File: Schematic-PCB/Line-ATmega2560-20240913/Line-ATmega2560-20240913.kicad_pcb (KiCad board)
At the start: 2 copper layers, 27 parts, among them J6 CH340E, J7 ICSP, SW1 SW_Push, U1 ATmega2560-16A, Y1 16MHz

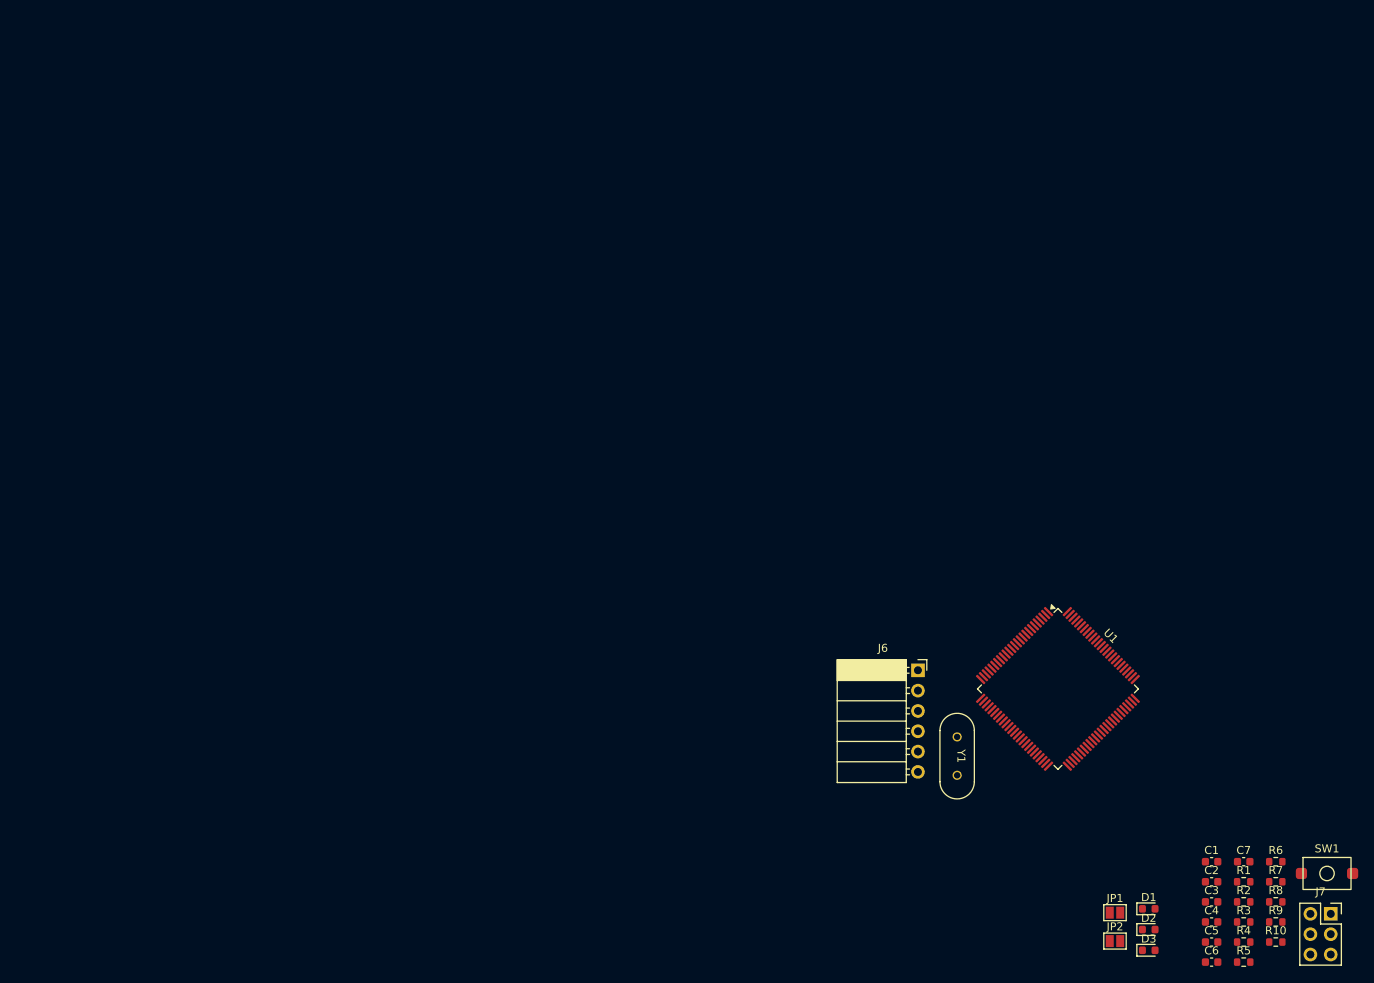
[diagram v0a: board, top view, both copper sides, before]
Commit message: 評価基板のPCB仮完成
各ピンを出す用のコネクタ以外は配置・配線完了
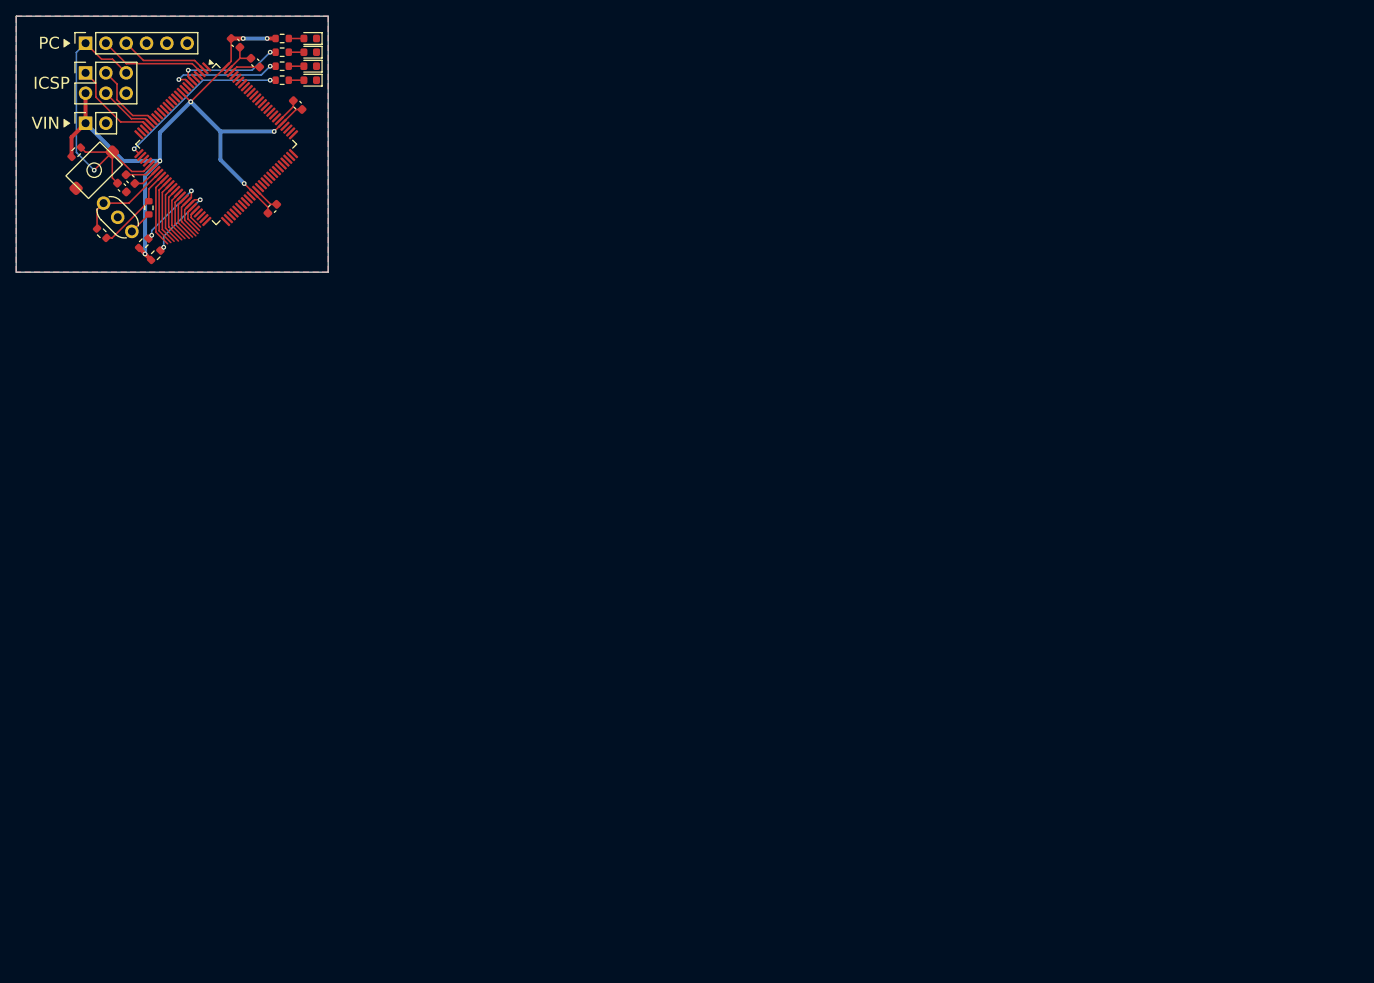
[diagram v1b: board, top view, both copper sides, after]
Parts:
- removed C7: 22p, Capacitor_SMD:C_0603_1608Metric
- removed J6: CH340E, Connector_PinSocket_2.54mm:PinSocket_1x06_P2.54mm_Horizontal
- removed J7: ICSP, Connector_PinSocket_2.54mm:PinSocket_2x03_P2.54mm_Vertical
- removed JP1: W_R, Jumper:SolderJumper-2_P1.3mm_Open_Pad1.0x1.5mm
- removed JP2: W/O_R, Jumper:SolderJumper-2_P1.3mm_Open_Pad1.0x1.5mm
- removed R10: 10K, Resistor_SMD:R_0603_1608Metric
- added D4: LED1, LED_SMD:LED_0603_1608Metric, F.Cu at (11.6, -8.29)
- added J10: VIN, Connector_PinSocket_2.54mm:PinSocket_1x02_P2.54mm_Vertical, F.Cu at (-16.4, -2.91)
- added J8: CH340E, Connector_PinSocket_2.54mm:PinSocket_1x06_P2.54mm_Vertical, F.Cu at (-16.4, -12.9)
- added J9: ICSP, Connector_PinSocket_2.54mm:PinSocket_2x03_P2.54mm_Vertical, F.Cu at (-16.4, -9.20)
- C6: value 22p -> 100n
- R7: value 10K -> 27
- R8: value 27R -> 330
- Y1: footprint @2024TOINIOT2-Line-ATmega2560:AL4BT -> Crystal:Resonator_Murata_CSTLSxxxX-3Pin_W5.5mm_H3.0mm
- moved SW1 177.4 mm to (-15.4, 2.96), turned to -135 degrees
- moved R2 173.4 mm to (-17.6, 0.71), turned to 45 degrees
- moved R9 170.1 mm to (-14.4, 10.8), turned to 135 degrees
- moved R5 164.3 mm to (-9.18, 12.1), turned to 45 degrees
- moved R7 164.1 mm to (-8.54, 7.67), turned to -90 degrees
- moved C4 164.0 mm to (-10.8, 4.07), turned to -45 degrees
- moved R4 162.6 mm to (8.13, -10.0)
- moved C3 162.5 mm to (2.30, -13.0), turned to -45 degrees
- moved R3 162.1 mm to (8.13, -11.8)
- moved C2 161.5 mm to (-11.9, 5.13), turned to -45 degrees
- moved R8 161.2 mm to (8.13, -8.29)
- moved R1 159.9 mm to (8.13, -13.5)
- moved R6 159.2 mm to (-7.68, 13.6), turned to 45 degrees
- moved C6 156.6 mm to (10.1, -5.18), turned to 135 degrees
- moved C1 155.8 mm to (4.77, -10.5), turned to -45 degrees
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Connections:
- C6 pad 1: Net-(JP2-B) -> +5V
- R7 pad 1: +5V -> XTAL1
- R7 pad 2: Net-(SW2-A) -> Net-(R7-Pad2)
- R8 pad 1: Net-(JP1-B) -> D13
- R8 pad 2: Net-(JP2-B) -> Net-(D4-A)
- R9 pad 1: Net-(JP2-B) -> XTAL1
- U1 pad 82: D42 -> ADC15
- U1 pad 83: D43 -> ADC14
- U1 pad 84: D44 -> ADC13
- U1 pad 85: D45 -> ADC12
- U1 pad 86: D46 -> ADC11
- U1 pad 87: D47 -> ADC10
- U1 pad 88: D48 -> ADC9
- U1 pad 89: D49 -> ADC8
- U1 pad 90: D9 -> ADC7
- U1 pad 91: D8 -> ADC6
- U1 pad 92: D7 -> ADC5
- U1 pad 93: D6 -> ADC4
- U1 pad 94: D9 -> ADC3
- U1 pad 95: D8 -> ADC2
- U1 pad 96: D7 -> ADC1
- U1 pad 97: D6 -> ADC0
- Y1 pad 1: XTAL2 -> Net-(R7-Pad2)
- Y1 pad 2: Net-(JP2-B) -> GND
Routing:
- net +5V: track 0.00 -> 94.9 mm, vias 0 -> 7
- net RESET: track 0.00 -> 41.5 mm, vias 0 -> 1
- net D13: track 0.00 -> 22.1 mm, vias 0 -> 2
- net SCL: track 0.00 -> 15.1 mm, vias 0 -> 2
- net SDA: track 0.00 -> 14.5 mm, vias 0 -> 2
- net GND: track 0.00 -> 14.5 mm
- net D3: track 0.00 -> 14.4 mm, vias 0 -> 2
- net D2: track 0.00 -> 13.4 mm, vias 0 -> 2
- net TX0: track 0.00 -> 13.4 mm
- net XTAL2: track 0.00 -> 12.0 mm
- net D50_MISO: track 0.00 -> 11.5 mm
- net RX0: track 0.00 -> 11.1 mm
- net XTAL1: track 0.00 -> 11.0 mm
- net D52_SCK: track 0.00 -> 9.53 mm
- net D49: track 0.00 -> 9.13 mm
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- added copper zone on B.Cu, net GND
- added copper zone on F.Cu, net GND
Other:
- board outline added: 39 x 32 mm
- board text added: "ICSP"
- board text added: "PC"
- board text added: "VIN"
